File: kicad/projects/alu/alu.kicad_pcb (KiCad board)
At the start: 2 copper layers, 203.2 x 97.8 mm, 49 parts, among them J1 ACC_CONTENTS, J2 RES_AEQB_CRYBRW_OUT, J3 Control_signal_backplane, J4 Bus_connection, J5 Aux_connection, U1 74HC04, U10 74HC157, U11 74HC157, U2 74LS181, U3 74LS181, U4 74HC245, U5 74LS181, U6 74HC245, U7 74LS181, U8 74HC157, U9 74HC157

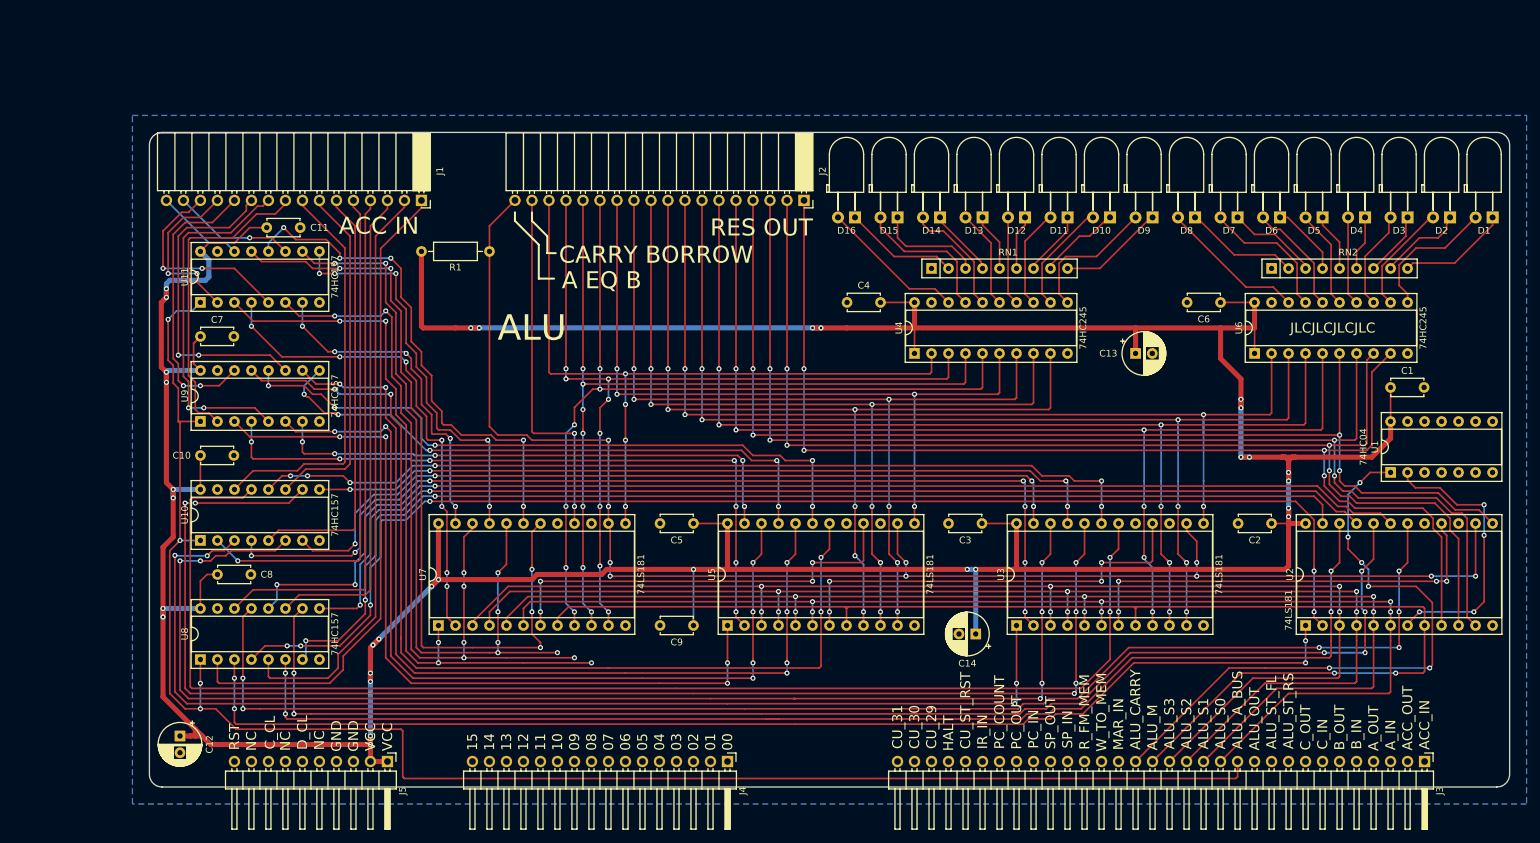
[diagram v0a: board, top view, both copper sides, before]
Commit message: Start adding ALU input buffers.
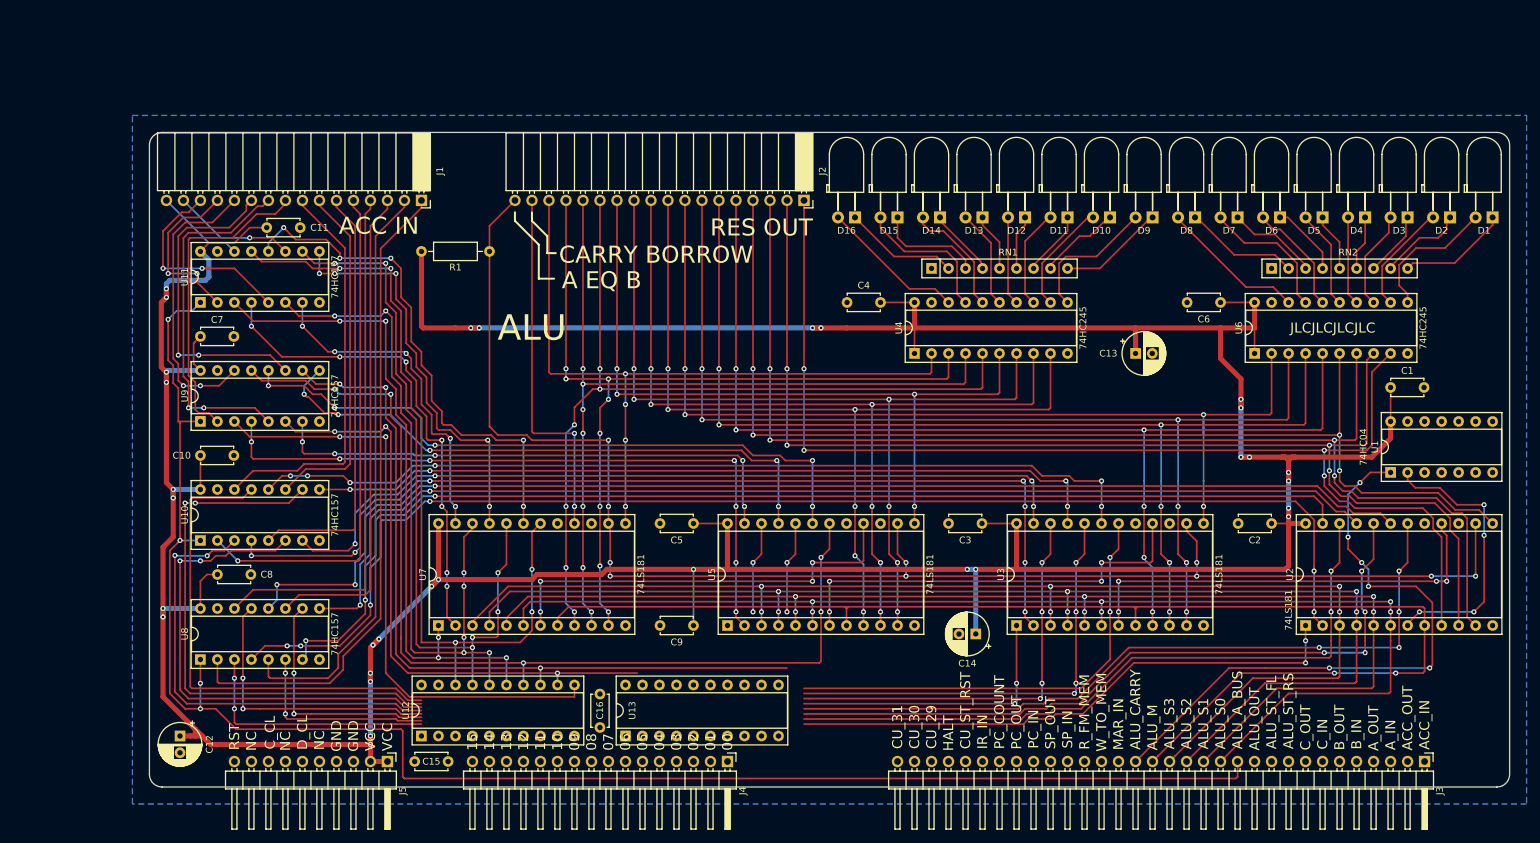
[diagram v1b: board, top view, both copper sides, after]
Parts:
- added C15: 0.1uF, Capacitor_THT:C_Disc_D4.7mm_W2.5mm_P5.00mm, F.Cu at (110.7, 157.5)
- added C16: 0.1uF, Capacitor_THT:C_Disc_D4.7mm_W2.5mm_P5.00mm, F.Cu at (138.4, 152.4)
- added U12: 74HC245, Package_DIP:DIP-20_W7.62mm_Socket, F.Cu at (111.8, 153.7)
- added U13: 74HC245, Package_DIP:DIP-20_W7.62mm_Socket, F.Cu at (142.2, 153.7)
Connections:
- U1 pad 3: GND -> /CARRY_BORROW_OUT_BAR
- U1 pad 4: Net-(U1-Pad4) -> /CARRY_BORROW_OUT
- U10 pad 10: /BUS_06 -> /BUS_BUF_06
- U10 pad 13: /BUS_07 -> /BUS_BUF_07
- U10 pad 3: /BUS_04 -> /BUS_BUF_04
- U10 pad 6: /BUS_05 -> /BUS_BUF_05
- U11 pad 10: /BUS_14 -> /BUS_BUF_14
- U11 pad 13: /BUS_15 -> /BUS_BUF_15
- U11 pad 3: /BUS_12 -> /BUS_BUF_12
- U11 pad 6: /BUS_13 -> /BUS_BUF_13
- U2 pad 1: /BUS_00 -> /BUS_BUF_00
- U2 pad 18: /BUS_03 -> /BUS_BUF_03
- U2 pad 20: /BUS_02 -> /BUS_BUF_02
- U2 pad 22: /BUS_01 -> /BUS_BUF_01
- U3 pad 1: /BUS_04 -> /BUS_BUF_04
- U3 pad 18: /BUS_07 -> /BUS_BUF_07
- U3 pad 20: /BUS_06 -> /BUS_BUF_06
- U3 pad 22: /BUS_05 -> /BUS_BUF_05
- U5 pad 1: /BUS_08 -> /BUS_BUF_08
- U5 pad 18: /BUS_11 -> /BUS_BUF_11
- U5 pad 20: /BUS_10 -> /BUS_BUF_10
- U5 pad 22: /BUS_09 -> /BUS_BUF_09
- U7 pad 1: /BUS_12 -> /BUS_BUF_12
- U7 pad 16: /CARRY_BORROW_OUT -> /CARRY_BORROW_OUT_BAR
- U7 pad 18: /BUS_15 -> /BUS_BUF_15
- U7 pad 20: /BUS_14 -> /BUS_BUF_14
- U7 pad 22: /BUS_13 -> /BUS_BUF_13
- U8 pad 10: /BUS_02 -> /BUS_BUF_02
- U8 pad 13: /BUS_03 -> /BUS_BUF_03
- U8 pad 3: /BUS_00 -> /BUS_BUF_00
- U8 pad 6: /BUS_01 -> /BUS_BUF_01
- U9 pad 10: /BUS_10 -> /BUS_BUF_10
- U9 pad 13: /BUS_11 -> /BUS_BUF_11
- U9 pad 3: /BUS_08 -> /BUS_BUF_08
- U9 pad 6: /BUS_09 -> /BUS_BUF_09
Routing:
- net /BUS_03: track 211.1 -> 0.00 mm, vias 6 -> 0
- net /BUS_06: track 205.2 -> 0.00 mm, vias 6 -> 0
- net /BUS_02: track 200.3 -> 0.00 mm, vias 6 -> 0
- net /BUS_07: track 197.9 -> 0.00 mm, vias 2 -> 0
- net /BUS_05: track 192.4 -> 0.00 mm, vias 6 -> 0
- net /BUS_01: track 191.0 -> 0.00 mm, vias 4 -> 0
- net /BUS_00: track 178.9 -> 0.00 mm, vias 4 -> 0
- net /BUS_04: track 168.2 -> 0.00 mm, vias 4 -> 0
- net /BUS_BUF_03: track 0.00 -> 154.3 mm, vias 0 -> 6
- net /BUS_BUF_11: track 0.00 -> 149.7 mm, vias 0 -> 5
- net /BUS_BUF_06: track 0.00 -> 148.7 mm, vias 0 -> 6
- net /BUS_11: track 147.4 -> 0.00 mm, vias 4 -> 0
- net /BUS_BUF_02: track 0.00 -> 143.4 mm, vias 0 -> 6
- net /BUS_BUF_07: track 0.00 -> 141.5 mm, vias 0 -> 2
- net /BUS_10: track 136.5 -> 0.00 mm, vias 6 -> 0
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
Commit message: Finish ALU input buffers.
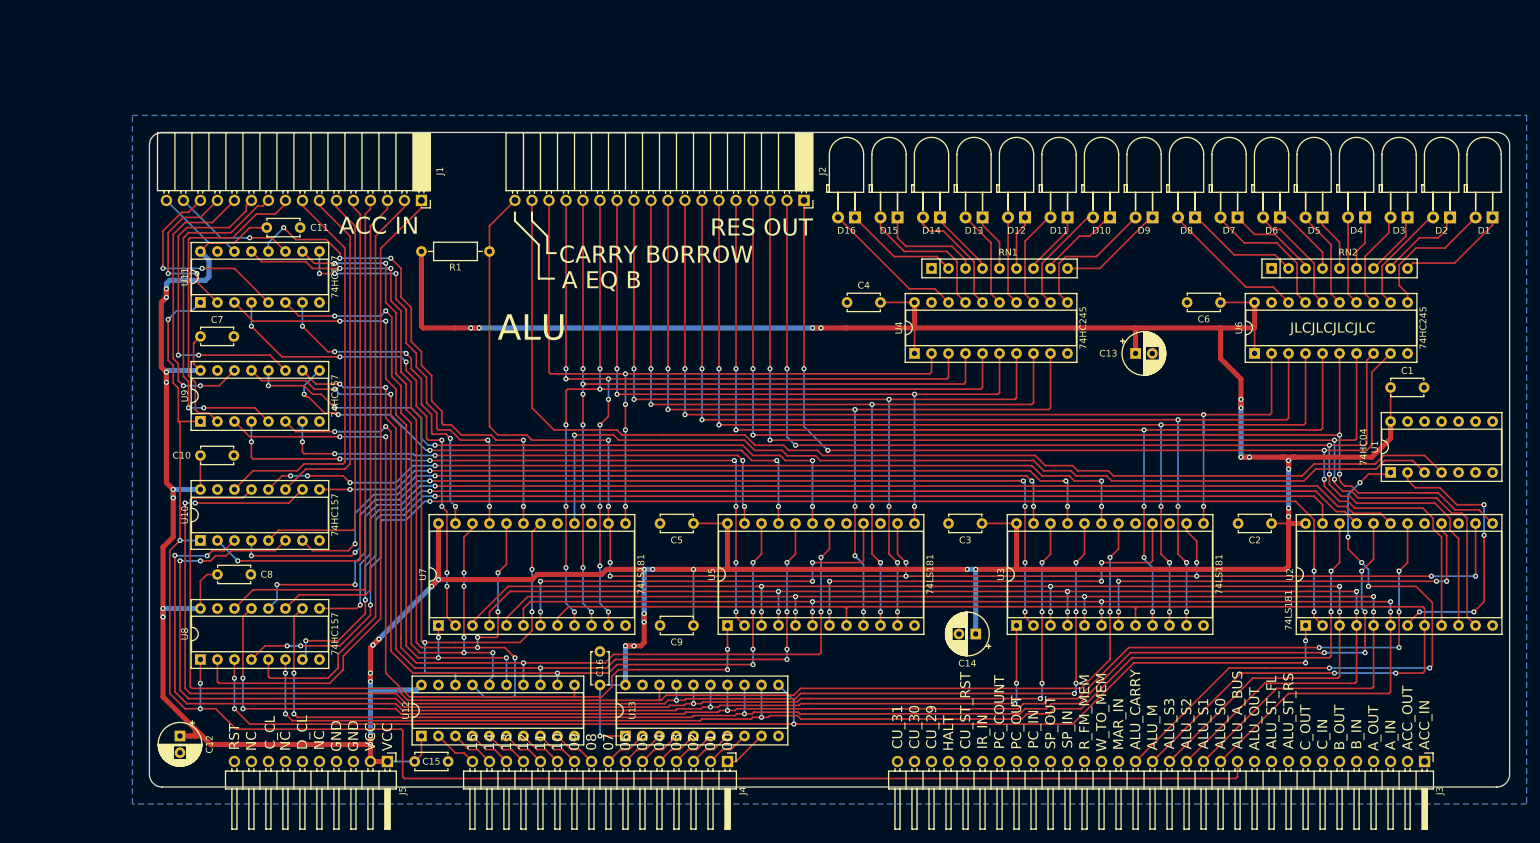
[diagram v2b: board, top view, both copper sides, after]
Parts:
- moved C16 6.35 mm to (138.4, 146.1)
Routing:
- net /CARRY_BORROW_OUT_BAR: track 0.00 -> 145.0 mm, vias 0 -> 1
- net /CARRY_BORROW_OUT: track 54.5 -> 173.4 mm, vias 2 -> 0
- net /BUS_BUF_00: track 121.7 -> 184.5 mm, vias 4 -> 5
- net /BUS_BUF_01: track 132.1 -> 194.3 mm, vias 4 -> 5
- net /BUS_BUF_02: track 143.4 -> 205.3 mm, vias 6 -> 7
- net /BUS_BUF_03: track 154.3 -> 215.6 mm, vias 6 -> 7
- net /BUS_BUF_04: track 111.5 -> 172.4 mm, vias 4 -> 5
- net /BUS_BUF_05: track 135.5 -> 196.0 mm, vias 6 -> 7
- net /BUS_BUF_07: track 141.5 -> 201.6 mm
- net /BUS_BUF_06: track 148.7 -> 208.8 mm, vias 6 -> 7
- net VCC: track 629.2 -> 683.0 mm, vias 31 -> 38
- net /BUS_BUF_08: track 90.3 -> 122.3 mm, vias 2 -> 4
- net /BUS_BUF_09: track 103.9 -> 129.2 mm, vias 5 -> 7
- net /BUS_BUF_14: track 108.9 -> 122.1 mm, vias 6 -> 7
- net /BUS_BUF_10: track 129.5 -> 136.7 mm, vias 5 -> 7
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
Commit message: Set LED drivers from ALU chips to HCTs.
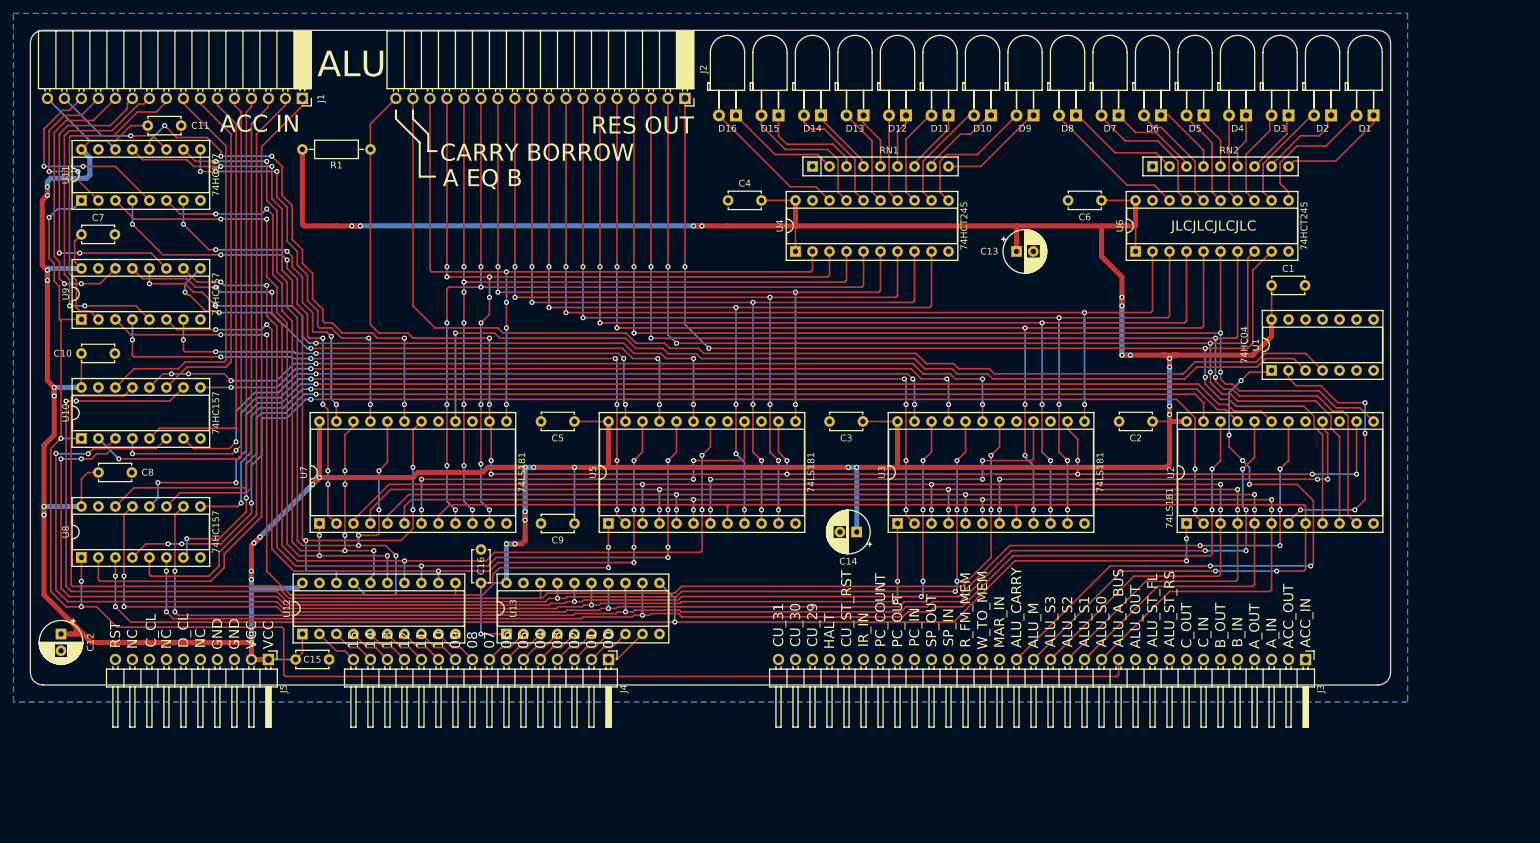
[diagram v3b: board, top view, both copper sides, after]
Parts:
- U4, U6: value 74HC245 -> 74HCT245
- moved C1 23.4 mm to (238.8, 86.4)
- moved U1 23.4 mm to (238.8, 99.1)
- moved C14 23.4 mm to (176.8, 123.2)
- moved C16 23.4 mm to (120.7, 130.8)
- moved C4 23.4 mm to (162.6, 73.7)
- moved C11 23.4 mm to (70.9, 62.5)
- moved D10 23.4 mm to (196.8, 61.0)
- moved D11 23.4 mm to (190.5, 61.0)
- moved D12 23.4 mm to (184.2, 61.0)
- moved D13 23.4 mm to (177.8, 61.0)
- moved D14 23.4 mm to (171.4, 61.0)
- moved D15 23.4 mm to (165.1, 61.0)
- moved D16 23.4 mm to (158.8, 61.0)
- moved D2 23.4 mm to (247.7, 61.0)
- moved D4 23.4 mm to (234.9, 61.0)
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
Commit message: Add top power and LED control jumper to ALU.
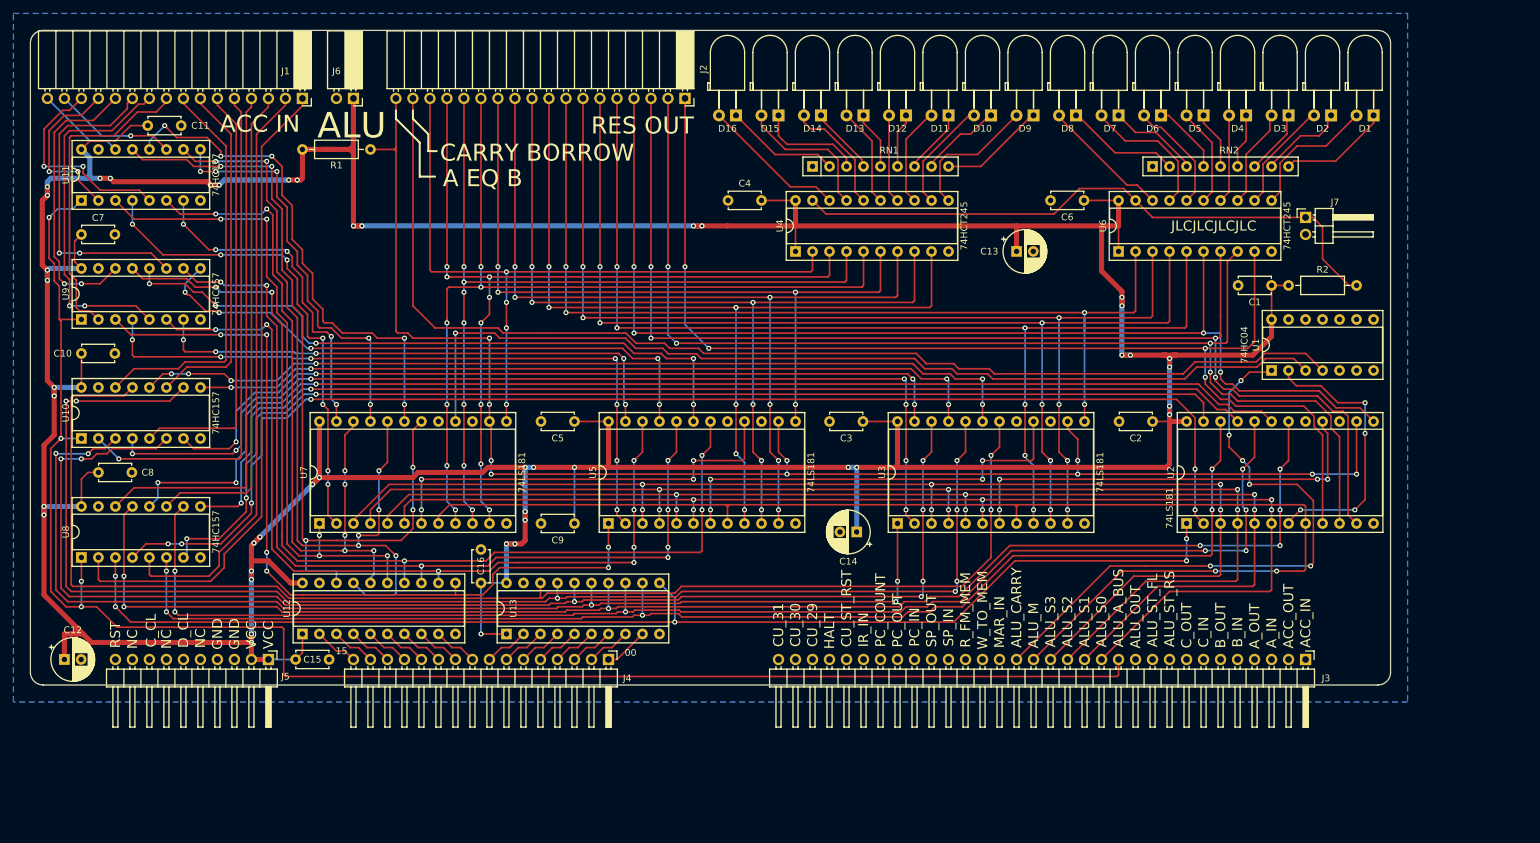
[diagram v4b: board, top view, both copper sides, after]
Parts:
- added J6: TOP_POWER, Connector_PinSocket_2.54mm:PinSocket_1x02_P2.54mm_Horizontal, F.Cu at (101.6, 58.4)
- added J7: LED_CONTROL, Connector_PinHeader_2.54mm:PinHeader_1x02_P2.54mm_Horizontal, F.Cu at (243.8, 76.2)
- added R2: 10K, Resistor_THT:R_Axial_DIN0207_L6.3mm_D2.5mm_P10.16mm_Horizontal, F.Cu at (241.3, 86.4)
- moved C12 3.84 mm to (58.4, 142.2), turned to 0 degrees
- moved C6 2.62 mm to (210.7, 73.7)
- moved U6 2.54 mm to (215.9, 81.3)
- turned C1 to 180 degrees
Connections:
- U4 pad 19: GND -> /LED_CONTROL
- U6 pad 19: GND -> /LED_CONTROL
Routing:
- net /LED_CONTROL: track 0.00 -> 92.5 mm
- net VCC: track 683.0 -> 735.0 mm, vias 38 -> 44
- net /RES_01: track 178.9 -> 176.1 mm
- net /RES_06: track 163.7 -> 161.2 mm
- net /RES_BUF_07: track 22.0 -> 19.5 mm
- net /RES_07: track 147.2 -> 144.6 mm
- net /RES_05: track 163.7 -> 161.2 mm
- net /RES_04: track 162.9 -> 160.4 mm
- net /RES_02: track 181.2 -> 178.6 mm
- net /RES_00: track 176.1 -> 175.1 mm
- net /ACC_13: track 30.9 -> 31.5 mm
- net /A_EQ_B: track 228.5 -> 228.0 mm
- net /BUS_BUF_08: vias 4 -> 6
